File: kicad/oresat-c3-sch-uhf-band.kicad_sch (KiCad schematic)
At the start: 126 parts, among them Q3 NTR4101, Q4 PMV45EN, U16 AX5043, U18 LT5534, U19 BDCN-20-13+, U20 QPC1022, U21 TQP7M9105, U22 LT5534, U25 SN74LVC1G11IDCKRQ1, U26 TLV7041DBV, U27 LP2985AIM5-1.8_NOPB, U29 TQP3M9036, U32 SF2446E, U33 SF2446E, U40 MAX941EUA+, X1 TYKTBLSANF-16.000000

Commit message: More progress on the UHF band radio.
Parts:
- U16: footprint (none) -> oresat-ics:U-AX5043-QFN28-5X5-WITH-CENTER-PAD
- U19: footprint (none) -> oresat-ics:BDCN-20-13+
- U21: footprint (none) -> oresat-ics:U-QORVO-TQP7M9105-PA_TQP7M9105
- U29: footprint (none) -> oresat-ics:U-Qorvo-TQP3M9036-QFN-8-MO-220E
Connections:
- net GND: now also U21.EP (GND), U29.EP (GND); no longer U21.4 (GND), U29. (GND)
- new net: U29.1, U29.3, U29.4, U29.8
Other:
- moved on the sheet: L8
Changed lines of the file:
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@@
     (stroke (width 0) (type default))
   )
-  (wire (pts (xy 259.08 226.06) (xy 252.73 226.06))
-    (stroke (width 0) (type default))
-  )
   (wire (pts (xy 368.3 180.34) (xy 368.3 181.61))
     (stroke (width 0) (type default))
@@
     (stroke (width 0) (type default))
   )
+  (wire (pts (xy 252.73 226.06) (xy 259.08 226.06))
+    (stroke (width 0) (type default))
+  )
   (wire (pts (xy 53.34 93.98) (xy 63.5 93.98))
     (stroke (width 0) (type default))
@@
       (effects (font (size 1.27 1.27)))
     )
-    (property "Footprint" "oresat-ics:SM3030-6" (at 306.07 220.98 0)
+    (property "Footprint" "oresat-ics:SM3030-6" (at 294.64 210.185 0)
       (effects (font (size 1.27 1.27)) hide)
     )
-    (property "Datasheet" "https://www.rfmi.co/pdf/Datasheet/sf2446e.pdf" (at 306.07 220.98 0)
+    (property "Datasheet" "https://www.rfmi.co/pdf/Datasheet/sf2446e.pdf" (at 294.64 207.645 0)
       (effects (font (size 1.27 1.27)) hide)
     )
@@
     )
   )
-  (symbol (lib_id "Device:R_Small_US") (at 254 215.9 0) (unit 1)
+  (symbol (lib_id "Device:R_Small_US") (at 254 215.9 0) (mirror y) (unit 1)
     (in_bom yes) (on_board yes) (dnp no)
-    (property "Reference" "R10" (at 255.27 215.265 0)
+    (property "Reference" "R10" (at 252.73 215.265 0)
       (effects (font (size 1.27 1.27)) (justify left))
     )
-    (property "Value" "33k" (at 255.27 217.805 0)
+    (property "Value" "33k" (at 252.73 217.805 0)
       (effects (font (size 1.27 1.27)) (justify left))
     )
@@
       (effects (font (size 1.27 1.27)))
     )
-    (property "Footprint" "" (at 302.26 91.44 0)
+    (property "Footprint" "oresat-ics:BDCN-20-13+" (at 302.26 91.44 0)
       (effects (font (size 1.27 1.27)) hide)
     )
@@
       (effects (font (size 1.27 1.27)) (justify left))
     )
-    (property "Footprint" "" (at 60.96 114.3 0)
+    (property "Footprint" "oresat-ics:U-AX5043-QFN28-5X5-WITH-CENTER-PAD" (at 60.96 114.3 0)
       (effects (font (size 1.27 1.27)) hide)
     )
@@
     )
   )
-  (symbol (lib_id "Device:L_Small") (at 234.95 218.44 0) (mirror y) (unit 1)
+  (symbol (lib_id "Device:L_Small") (at 234.95 218.44 0) (unit 1)
     (in_bom yes) (on_board yes) (dnp no)
-    (property "Reference" "L8" (at 232.41 217.17 0)
+    (property "Reference" "L8" (at 237.49 217.17 0)
       (effects (font (size 1.27 1.27)))
     )
-    (property "Value" "68n" (at 232.41 219.71 0)
+    (property "Value" "68n" (at 237.49 219.71 0)
       (effects (font (size 1.27 1.27)))
     )
@@
       (effects (font (size 1.27 1.27)))
     )
-    (property "Footprint" "" (at 227.33 93.98 0)
+    (property "Footprint" "oresat-ics:U-QORVO-TQP7M9105-PA_TQP7M9105" (at 227.33 93.98 0)
       (effects (font (size 1.27 1.27)) hide)
     )
@@
     (pin "2")
     (pin "3")
-    (pin "4")
+    (pin "EP")
     (instances
       (project "oresat-c3"
@@
       (effects (font (size 1.27 1.27)))
     )
-    (property "Footprint" "" (at 251.46 217.17 0)
+    (property "Footprint" "oresat-ics:U-Qorvo-TQP3M9036-QFN-8-MO-220E" (at 251.46 217.17 0)
       (effects (font (size 1.27 1.27)) hide)
     )
-    (property "Datasheet" "https://www.mouser.com/datasheet/2/412/TQP3M9036_Data_Sheet-1500677.pdf" (at 251.46 217.17 0)
+    (property "Datasheet" "https://www.qorvo.com/products/d/da005543" (at 251.46 217.17 0)
       (effects (font (size 1.27 1.27)) hide)
     )
-    (pin "")
+    (pin "1")
     (pin "2")
+    (pin "3")
+    (pin "4")
     (pin "6")
     (pin "7")
+    (pin "8")
+    (pin "EP")
     (instances
       (project "oresat-c3"

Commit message: Fixed footprints and laid out WDT and OPD circuitry.
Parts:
- AT1, AT2, AT3, AT4: footprint (none) -> oresat-passives:PAT0816(0603); symbol oresat-passives:Attenuator -> oresat-passives:PAT0816-attenuator
- U18, U22: footprint (none) -> Package_TO_SOT_SMD:SOT-363_SC-70-6
- U26: footprint (none) -> Package_TO_SOT_SMD:TSOT-23-8
- X1: footprint (none) -> oresat-ics:X_TCXO_SMD_Taitien_2.5x2.0mm; symbol oresat-ics:TAITIEN-TY -> oresat-ics:Taiten-TY-Series-TXCO
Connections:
- net UHF_TOT_CLEAR: now also D1.2; no longer D1. (2)
- net at R115.2, U40.5 (~{LATCH}): now also D1.1; no longer D1. (2)
- net UHF_FWD_LOG_RF renamed UHF_FWD_RF_LOG
- net UHF_REV_LOG_RF renamed UHF_REV_RF_LOG

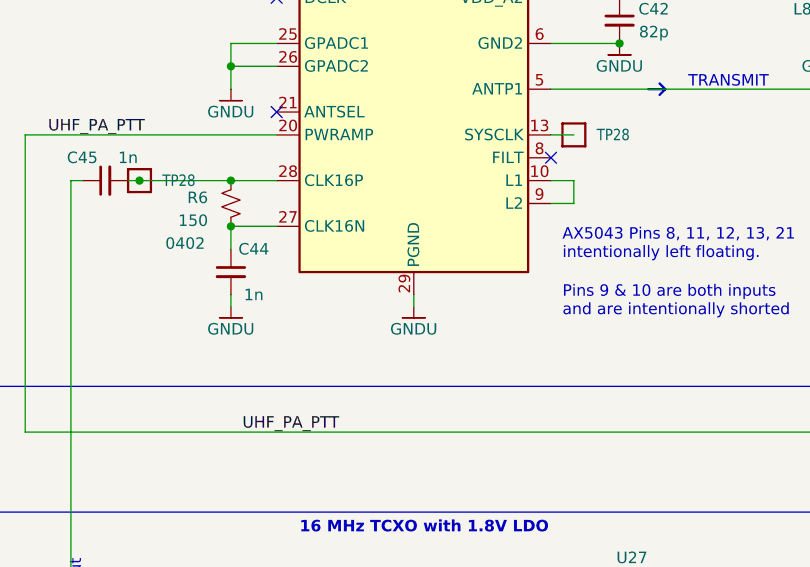
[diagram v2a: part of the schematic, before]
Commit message: More progress on C3 v6. All ICs and Packages are in, deployer and power supply and I2C subsystems laid out.
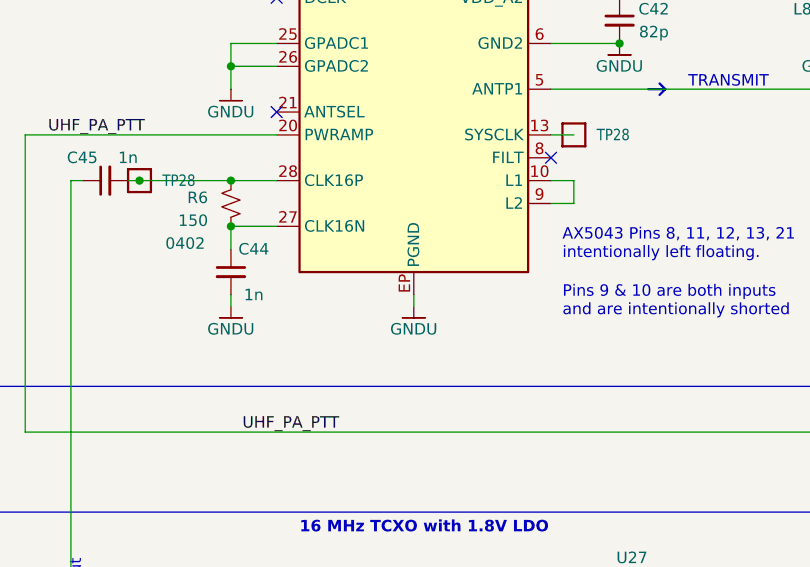
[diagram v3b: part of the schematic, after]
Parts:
- Q3, Q4: footprint (none) -> Package_TO_SOT_SMD:SOT-23-3
- U25: footprint (none) -> Package_TO_SOT_SMD:Texas_R-PDSO-G6
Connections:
- net GND: now also U16.EP (PGND); no longer U16.29 (PGND)
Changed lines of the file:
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@@
       (effects (font (size 1.27 1.27)))
     )
-    (property "Footprint" "" (at 250.19 121.92 0)
+    (property "Footprint" "Package_TO_SOT_SMD:SOT-23-3" (at 250.19 121.92 0)
       (effects (font (size 1.27 1.27)) hide)
     )
@@
       (effects (font (size 1.27 1.27)) (justify left))
     )
-    (property "Footprint" "" (at 238.76 129.54 0)
+    (property "Footprint" "Package_TO_SOT_SMD:SOT-23-3" (at 238.76 129.54 0)
       (effects (font (size 1.27 1.27)) hide)
     )
@@
       (effects (font (size 1.27 1.27)) (justify right))
     )
-    (property "Footprint" "" (at 213.36 160.02 0)
+    (property "Footprint" "Package_TO_SOT_SMD:Texas_R-PDSO-G6" (at 213.36 160.02 0)
       (effects (font (size 1.27 1.27)) hide)
     )
@@
     (pin "27")
     (pin "28")
-    (pin "29")
     (pin "3")
     (pin "4")
@@
     (pin "8")
     (pin "9")
-    (instances
-      (project "oresat-c3"
+    (pin "EP")
+    (instances
+      (project "oresat-c3"

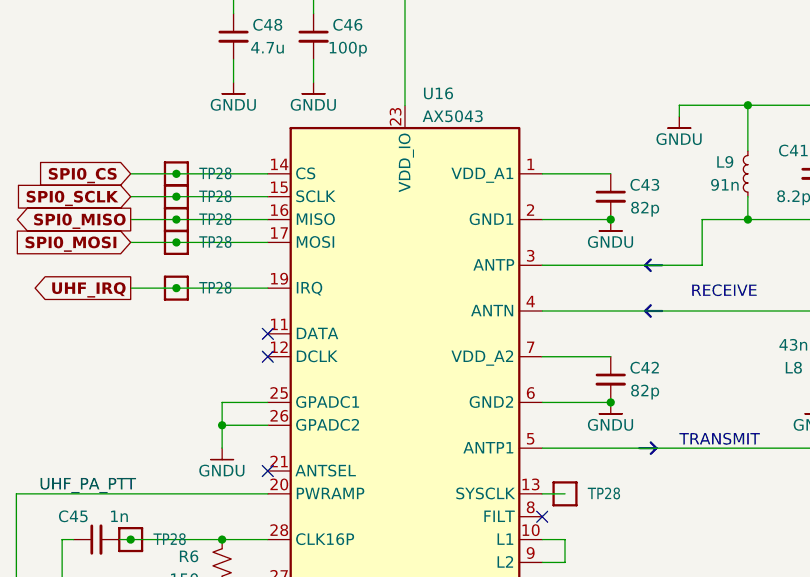
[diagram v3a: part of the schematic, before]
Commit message: routed everything but some minor lines and the radios. About to move the octavo and EVERYTHING else, wish me luck. Should give enough room for the radios!
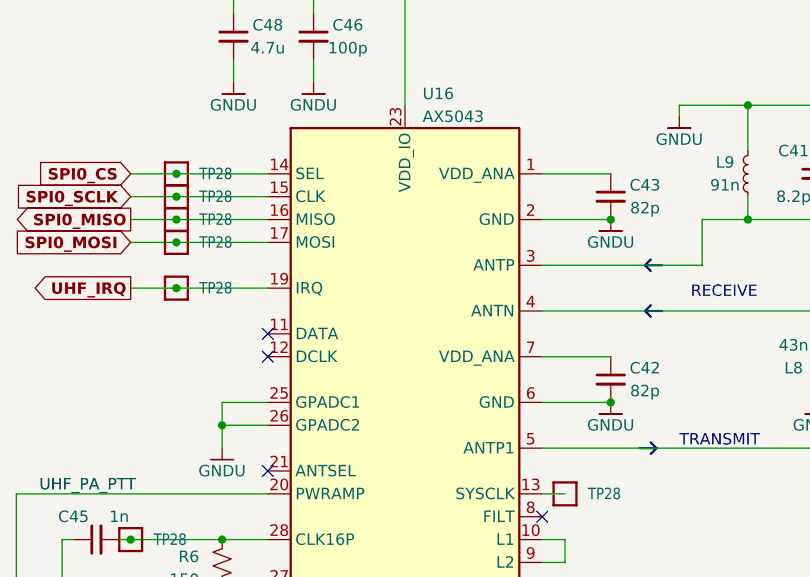
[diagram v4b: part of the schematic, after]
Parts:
- U26: footprint Package_TO_SOT_SMD:TSOT-23-8 -> Package_TO_SOT_SMD:SOT-23-5
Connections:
- net at U29.1 (NC), U29.3 (NC), U29.4 (NC)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: now also U29.5 (NC)
- new net: U16.18 (NC), U16.22 (NC), U16.24 (NC)
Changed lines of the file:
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@@
       (effects (font (size 1.27 1.27)))
     )
-    (property "Footprint" "Package_TO_SOT_SMD:TSOT-23-8" (at 119.38 57.15 0)
+    (property "Footprint" "Package_TO_SOT_SMD:SOT-23-5" (at 119.38 57.15 0)
       (effects (font (size 1.27 1.27)) hide)
     )
@@
       (effects (font (size 1.27 1.27)) hide)
     )
-    (property "Datasheet" "" (at 60.96 114.3 0)
+    (property "Datasheet" "https://www.mouser.com/datasheet/2/308/AX5043-D-782042.pdf" (at 60.96 114.3 0)
       (effects (font (size 1.27 1.27)) hide)
     )
+    (pin "18")
+    (pin "22")
+    (pin "24")
     (pin "1")
     (pin "10")
@@
       (effects (font (size 1.27 1.27)) hide)
     )
+    (pin "5")
     (pin "1")
     (pin "2")

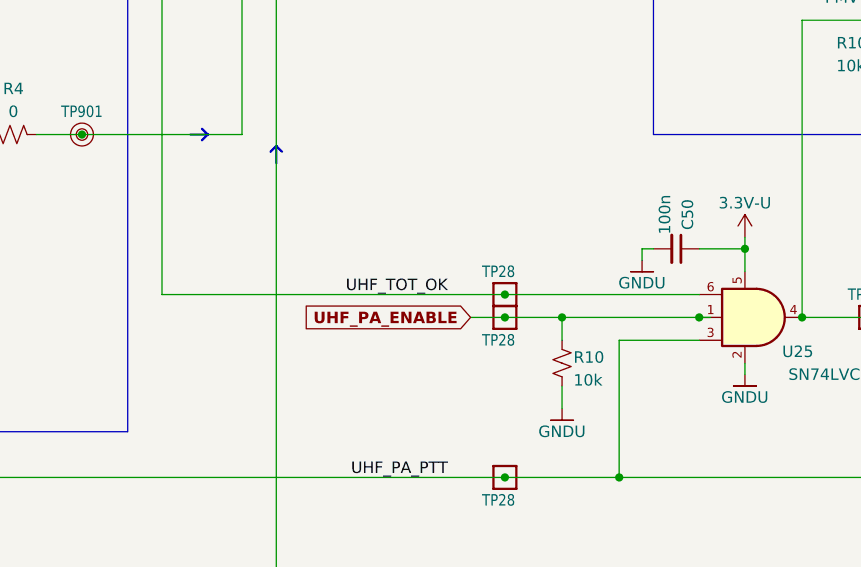
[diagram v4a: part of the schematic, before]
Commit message: Rough draft layout of UHF radio. Fixed duplicated test points.
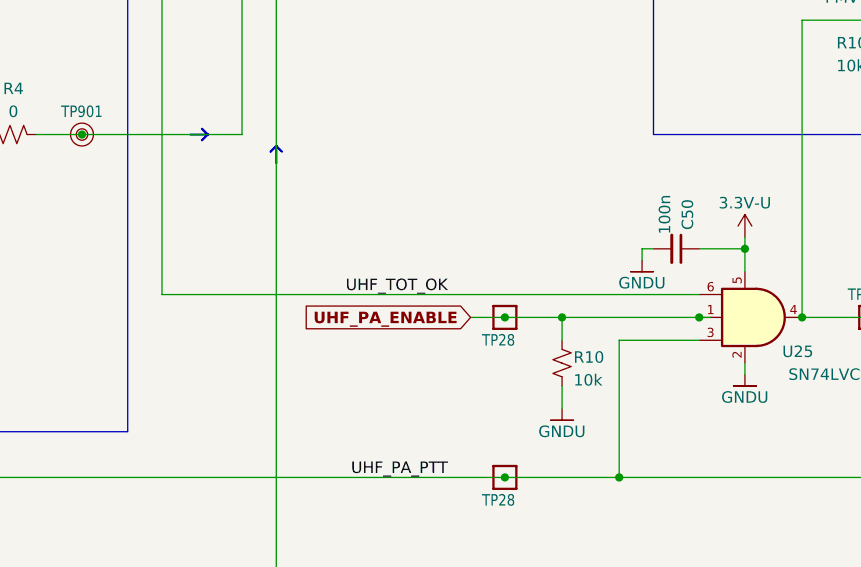
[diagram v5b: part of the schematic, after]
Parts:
- removed TP28: Test-Point, oresat-misc:TestPoint_Pad_D1.0mm, symbol oresat-misc:Test-Point-1mm-round
- R10: footprint Resistor_SMD:R_0402_1005Metric -> Resistor_SMD:R_0603_1608Metric
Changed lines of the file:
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@@
   (junction (at 199.39 182.88) (diameter 0) (color 0 0 0 0)
   )
-  (junction (at 186.69 162.56) (diameter 0) (color 0 0 0 0)
-  )
   (junction (at 38.1 114.3) (diameter 0) (color 0 0 0 0)
   )
@@
     (stroke (width 0) (type default))
   )
-  (wire (pts (xy 186.69 162.56) (xy 208.28 162.56))
+  (wire (pts (xy 148.59 162.56) (xy 208.28 162.56))
     (stroke (width 0) (type default))
   )
@@
     (stroke (width 0) (type default))
   )
-  (wire (pts (xy 148.59 162.56) (xy 186.69 162.56))
-    (stroke (width 0) (type default))
-  )
   (wire (pts (xy 335.28 53.34) (xy 340.36 53.34))
     (stroke (width 0) (type default))
@@
       (effects (font (size 1.27 1.27)) (justify left))
     )
-    (property "Footprint" "Resistor_SMD:R_0402_1005Metric" (at 83.82 38.1 0)
+    (property "Footprint" "Resistor_SMD:R_0603_1608Metric" (at 83.82 38.1 0)
       (effects (font (size 1.27 1.27)) hide)
     )
@@
       (effects (font (size 1.27 1.27)) (justify left))
     )
-    (property "Footprint" "Resistor_SMD:R_0402_1005Metric" (at 132.08 45.72 0)
+    (property "Footprint" "Resistor_SMD:R_0603_1608Metric" (at 132.08 45.72 0)
       (effects (font (size 1.27 1.27)) hide)
     )
@@
       (effects (font (size 1.27 1.27)) (justify left))
     )
-    (property "Footprint" "Resistor_SMD:R_0402_1005Metric" (at 132.08 53.34 0)
+    (property "Footprint" "Resistor_SMD:R_0603_1608Metric" (at 132.08 53.34 0)
       (effects (font (size 1.27 1.27)) hide)
     )
@@
     )
   )
-  (symbol (lib_id "oresat-misc:Test-Point-1mm-round") (at 186.69 162.56 90) (unit 1)
-    (in_bom yes) (on_board yes) (dnp no)
-    (property "Reference" "TP28" (at 184.15 160.02 90)
-      (effects (font (size 1.27 1.0795)) (justify right))
-    )
-    (property "Value" "Test-Point" (at 179.07 162.56 0)
-      (effects (font (size 1.27 1.27)) hide)
-    )
-    (property "Footprint" "oresat-misc:TestPoint_Pad_D1.0mm" (at 176.53 162.56 0)
-      (effects (font (size 1.27 1.27)) hide)
-    )
-    (property "Datasheet" "" (at 186.69 162.56 0)
-      (effects (font (size 1.27 1.27)) hide)
-    )
-    (pin "1")
-    (instances
-      (project "oresat-c3"
-        (path "/65d12cdd-c326-4033-9053-c59fa4e0b25e/1b68ea4b-cacf-4529-b1d4-9be5d7c1043c"
-          (reference "TP28") (unit 1)
-        )
-        (path "/65d12cdd-c326-4033-9053-c59fa4e0b25e/05e45903-5042-4bc1-87af-e9d7510ea02d"
-          (reference "TP58") (unit 1)
-        )
-      )
-    )
-  )
   (symbol (lib_id "oresat-power:3.3V-U") (at 132.08 41.91 0) (unit 1)
     (in_bom yes) (on_board yes) (dnp no) (fields_autoplaced)
@@
       (effects (font (size 1.27 1.27)) (justify left))
     )
-    (property "Footprint" "Resistor_SMD:R_0402_1005Metric" (at 96.52 43.18 0)
+    (property "Footprint" "Resistor_SMD:R_0603_1608Metric" (at 96.52 43.18 0)
       (effects (font (size 1.27 1.27)) hide)
     )
@@
       (effects (font (size 1.27 1.27)) (justify left))
     )
-    (property "Footprint" "Resistor_SMD:R_0402_1005Metric" (at 83.82 30.48 0)
+    (property "Footprint" "Resistor_SMD:R_0603_1608Metric" (at 83.82 30.48 0)
       (effects (font (size 1.27 1.27)) hide)
     )
